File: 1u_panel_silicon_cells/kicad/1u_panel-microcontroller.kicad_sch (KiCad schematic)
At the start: 43 parts, among them J2 2-1734592-0, U1 TCAN330GDCNT, U11 TMP101NA/3KSLOTTED, U2 TMP101NA/3KSLOTTED, U7 STM32F091CCT7, X1 ECS-160-10-36Q-ES-TR

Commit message: fixed board outline, title blocks
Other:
- title: OreSat Solar Module (for Frame 2.0) -> OreSat Silicon Solar Module (for Frame 2.0)
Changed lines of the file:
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@@
 	(paper "USLedger")
 	(title_block
-		(title "OreSat Solar Module (for Frame 2.0)")
-		(date "2023-12-20")
-		(rev "6.0")
+		(title "OreSat Silicon Solar Module (for Frame 2.0)")
+		(date "2024-08-18")
+		(rev "1.0")
 	)
 	(junction

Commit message: updating remote repo for design review
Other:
- note added: "Solar module ID Required by CAN messages. 0: +X+Z 1: -Y+Z 2: -X+Z 3: -Y+Z 4: +X-Z .. and so on."
- note removed: "Solar module Serial Number Required by CAN messages. 0: +X+Z 1: -Y+Z 2: -X+Z 3: -Y+Z 4: +X-Z .. and so on."
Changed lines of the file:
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@@
 		)
 	)
-	(text "Solar module Serial Number\nRequired by CAN messages.\n0: +X+Z\n1: -Y+Z\n2: -X+Z\n3: -Y+Z\n4: +X-Z\n.. and so on."
+	(text "Solar module ID\nRequired by CAN messages.\n0: +X+Z\n1: -Y+Z\n2: -X+Z\n3: -Y+Z\n4: +X-Z\n.. and so on."
 		(exclude_from_sim no)
 		(at 226.06 215.9 0)

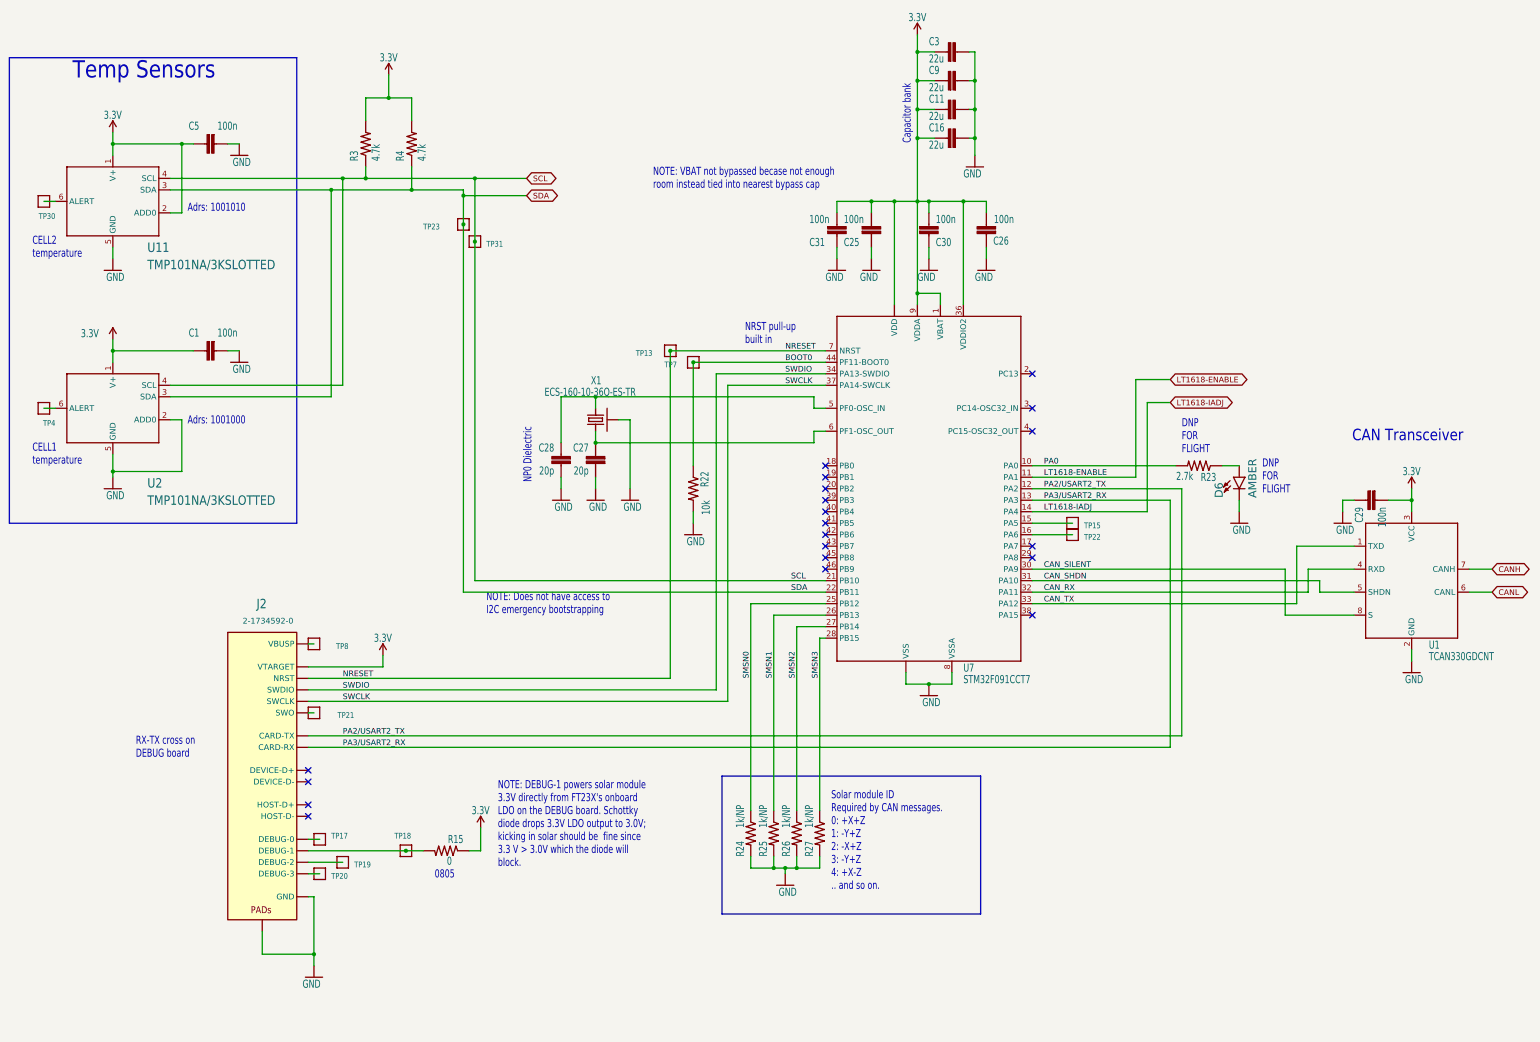
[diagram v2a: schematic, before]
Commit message: commiting silicon solar panel before moving programming header
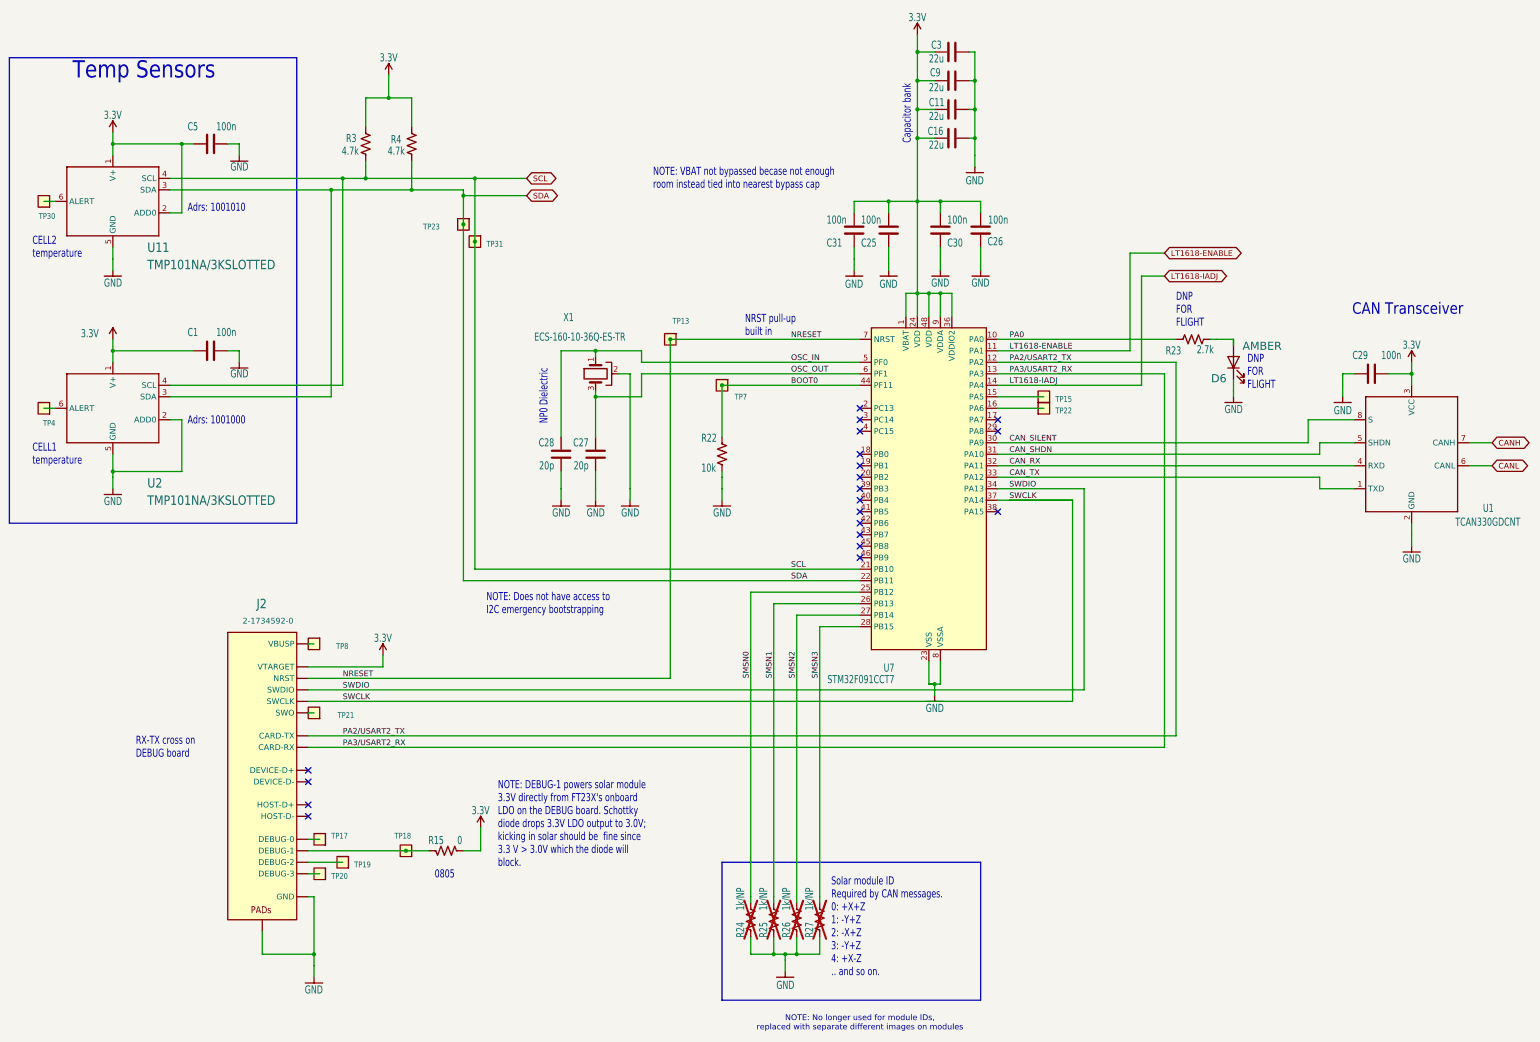
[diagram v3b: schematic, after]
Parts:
- C1, C25, C26, C27, C28, C29, C30, C31, C5: footprint 1u_panel:.0603-C-NOSILK -> oresat-passives:0603-C-NOSILK; symbol 1u_panel-eagle-import:oresat-rcl_C-EU0603-C-NOSILK -> Device:C
- C11, C16, C3, C9: footprint 1u_panel:.0805-B-NOSILK -> oresat-passives:0805-C-NOSILK; symbol 1u_panel-eagle-import:oresat-rcl_C-EU0805-B-NOSILK -> Device:C; DPN 1276-6817-1-ND -> 2571-GMC21X7R226M10NTTR-ND; MFR Samsung -> Cal-Chip; MPN CL32B226KOJVPNE -> GMC21X7R226M10NT
- D6: footprint 1u_panel:LED-0603 -> oresat-diodes:LED-0603; symbol 1u_panel-eagle-import:LED-GREEN0603 -> Device:LED
- R15: footprint 1u_panel:.0805-C-NOSILK -> oresat-passives:0805-C-NOSILK; symbol 1u_panel-eagle-import:R-US_0805-C-NOSILK -> Device:R_US
- R22: footprint 1u_panel:.0603-C-NOSILK -> oresat-passives:0603-C-NOSILK; symbol 1u_panel-eagle-import:R-US_0603-C-NOSILK -> Device:R_US; DPN A129693CT-ND -> RMCF0603JT10K0; MFR TE -> Stackpole; MPN CRGCQ0603F2K7 -> RMCF0603JT10K0
- R23, R3, R4: footprint 1u_panel:.0603-C-NOSILK -> oresat-passives:0603-C-NOSILK; symbol 1u_panel-eagle-import:R-US_0603-C-NOSILK -> Device:R_US
- R24, R25, R26, R27: footprint 1u_panel:.0603-C-NOSILK -> oresat-passives:0603-C-NOSILK; symbol 1u_panel-eagle-import:R-US_0603-C-NOSILK -> Device:R_US; now not fitted
- TP13, TP15, TP17, TP18, TP19, TP20, TP21, TP22, TP23, TP30, TP31, TP4, TP7, TP8: footprint 1u_panel:1X01 -> oresat-misc:TestPoint-0.75mm-th; symbol 1u_panel-eagle-import:TEST-POINT-LARGE-SQUARE -> oresat-misc:Test-Point-0.75mm-th; now left out of the parts list
- U1: footprint 1u_panel:SOT23-8_TI-DCN -> oresat-ics:SOT23-8_TI-DCN; symbol 1u_panel-eagle-import:TCAN330 -> oresat-ics:TCAN330; Distributor (none) -> DigiKey; MPN TCAN330GDCNT -> TCAN330GDCN
- U11, U2: footprint 1u_panel:DBV6-SLOT -> oresat-ics:DBV6-SLOT; symbol 1u_panel-eagle-import:TMP101NA/3KSLOTTED -> oresat-ics:TMP101NA
- U7: footprint 1u_panel:STM32F091C -> Package_QFP:LQFP-48_7x7mm_P0.5mm; symbol 1u_panel-eagle-import:STM32F091C -> MCU_ST_STM32F0:STM32F091CCUx
- X1: footprint 1u_panel:CRYSTAL_2.5X2 -> Crystal:Crystal_SMD_2520-4Pin_2.5x2.0mm; symbol 1u_panel-eagle-import:CRYSTAL-WITH-GND -> Device:Crystal_GND2
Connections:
- net 3.3V: now also R15.2; no longer R15.1
- net GND: no longer X1.4 (SHIELD)
- net at J2.18 (DEBUG-1), TP18.1: now also R15.1; no longer R15.2
- net OSC_IN: now reaches C28.1, U7.5 (PF0), X1.1
- net OSC_OUT: now reaches C27.1, U7.6 (PF1), X1.3
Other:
- note added: "NOTE: No longer used for module IDs, replaced with separate different images on modules"
- moved on the sheet: U1

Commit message: Updated all PN/DS/DPN/MPN/etc. for silicon solar module components
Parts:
- C1, C25, C26, C29, C30, C31, C5: DPN 1276-6985-1-ND -> 490-5798-2-ND; MFR Kemet -> Murata; MPN CL10B104KB85PND -> GCJ188R71H104KA12D
- C27, C28: DPN 490-11157-2-ND -> 490-1334-2-ND; MPN GCM1885C2A200JA16D -> GRM1885C2A200JA01D
- J2: DPN 732-11341-1-ND -> A100287TR-ND; MFR Wurth -> TE; MPN 687120183622 -> 2-1734592-0
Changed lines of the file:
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@@
 			)
 		)
-		(property "DPN" "732-11341-1-ND"
+		(property "DPN" "A100287TR-ND"
 			(at 100.33 189.23 0)
 			(effects
@@
 			)
 		)
-		(property "MFR" "Wurth"
+		(property "MFR" "TE"
 			(at 100.33 189.23 0)
 			(effects
@@
 			)
 		)
-		(property "MPN" "687120183622  "
+		(property "MPN" "2-1734592-0"
 			(at 100.33 189.23 0)
 			(effects
@@
 			)
 		)
-		(property "DPN" "1276-6985-1-ND"
+		(property "DPN" "490-5798-2-ND"
 			(at 88.9 50.8 0)
 			(effects
@@
 			)
 		)
-		(property "MFR" "Kemet"
+		(property "MFR" "Murata"
 			(at 88.9 50.8 0)
 			(effects
@@
 			)
 		)
-		(property "MPN" "CL10B104KB85PND"
+		(property "MPN" "GCJ188R71H104KA12D"
 			(at 88.9 50.8 0)
 			(effects
@@
 			)
 		)
-		(property "DPN" "1276-6985-1-ND"
+		(property "DPN" "490-5798-2-ND"
 			(at 231.14 69.85 0)
 			(effects
@@
 			)
 		)
-		(property "MFR" "Kemet"
+		(property "MFR" "Murata"
 			(at 231.14 69.85 0)
 			(effects
@@
 			)
 		)
-		(property "MPN" "CL10B104KB85PND"
+		(property "MPN" "GCJ188R71H104KA12D"
 			(at 231.14 69.85 0)
 			(effects
@@
 			)
 		)
-		(property "DPN" "490-11157-2-ND"
+		(property "DPN" "490-1334-2-ND"
 			(at 166.37 119.38 0)
 			(effects
@@
 			)
 		)
-		(property "MPN" "GCM1885C2A200JA16D"
+		(property "MPN" "GRM1885C2A200JA01D"
 			(at 166.37 119.38 0)
 			(effects
@@
 			)
 		)
-		(property "DPN" "1276-6985-1-ND"
+		(property "DPN" "490-5798-2-ND"
 			(at 88.9 96.52 0)
 			(effects
@@
 			)
 		)
-		(property "MFR" "Kemet"
+		(property "MFR" "Murata"
 			(at 88.9 96.52 0)
 			(effects
@@
 			)
 		)
-		(property "MPN" "CL10B104KB85PND"
+		(property "MPN" "GCJ188R71H104KA12D"
 			(at 88.9 96.52 0)
 			(effects
@@
 			)
 		)
-		(property "DPN" "1276-6985-1-ND"
+		(property "DPN" "490-5798-2-ND"
 			(at 250.19 69.85 0)
 			(effects
@@
 			)
 		)
-		(property "MFR" "Kemet"
+		(property "MFR" "Murata"
 			(at 250.19 69.85 0)
 			(effects
@@
 			)
 		)
-		(property "MPN" "CL10B104KB85PND"
+		(property "MPN" "GCJ188R71H104KA12D"
 			(at 250.19 69.85 0)
 			(effects
@@
 			)
 		)
-		(property "DPN" "490-11157-2-ND"
+		(property "DPN" "490-1334-2-ND"
 			(at 173.99 119.38 0)
 			(effects
@@
 			)
 		)
-		(property "MPN" "GCM1885C2A200JA16D"
+		(property "MPN" "GRM1885C2A200JA01D"
 			(at 173.99 119.38 0)
 			(effects
@@
 			)
 		)
-		(property "DPN" "1276-6985-1-ND"
+		(property "DPN" "490-5798-2-ND"
 			(at 345.44 101.6 0)
 			(effects
@@
 			)
 		)
-		(property "MFR" "Kemet"
+		(property "MFR" "Murata"
 			(at 345.44 101.6 0)
 			(effects
@@
 			)
 		)
-		(property "MPN" "CL10B104KB85PND"
+		(property "MPN" "GCJ188R71H104KA12D"
 			(at 345.44 101.6 0)
 			(effects
@@
 			)
 		)
-		(property "DPN" "1276-6985-1-ND"
+		(property "DPN" "490-5798-2-ND"
 			(at 238.76 69.85 0)
 			(effects
@@
 			)
 		)
-		(property "MFR" "Kemet"
+		(property "MFR" "Murata"
 			(at 238.76 69.85 0)
 			(effects
@@
 			)
 		)
-		(property "MPN" "CL10B104KB85PND"
+		(property "MPN" "GCJ188R71H104KA12D"
 			(at 238.76 69.85 0)
 			(effects
@@
 			)
 		)
-		(property "DPN" "1276-6985-1-ND"
+		(property "DPN" "490-5798-2-ND"
 			(at 259.08 69.85 0)
 			(effects
@@
 			)
 		)
-		(property "MFR" "Kemet"
+		(property "MFR" "Murata"
 			(at 259.08 69.85 0)
 			(effects
@@
 			)
 		)
-		(property "MPN" "CL10B104KB85PND"
+		(property "MPN" "GCJ188R71H104KA12D"
 			(at 259.08 69.85 0)
 			(effects

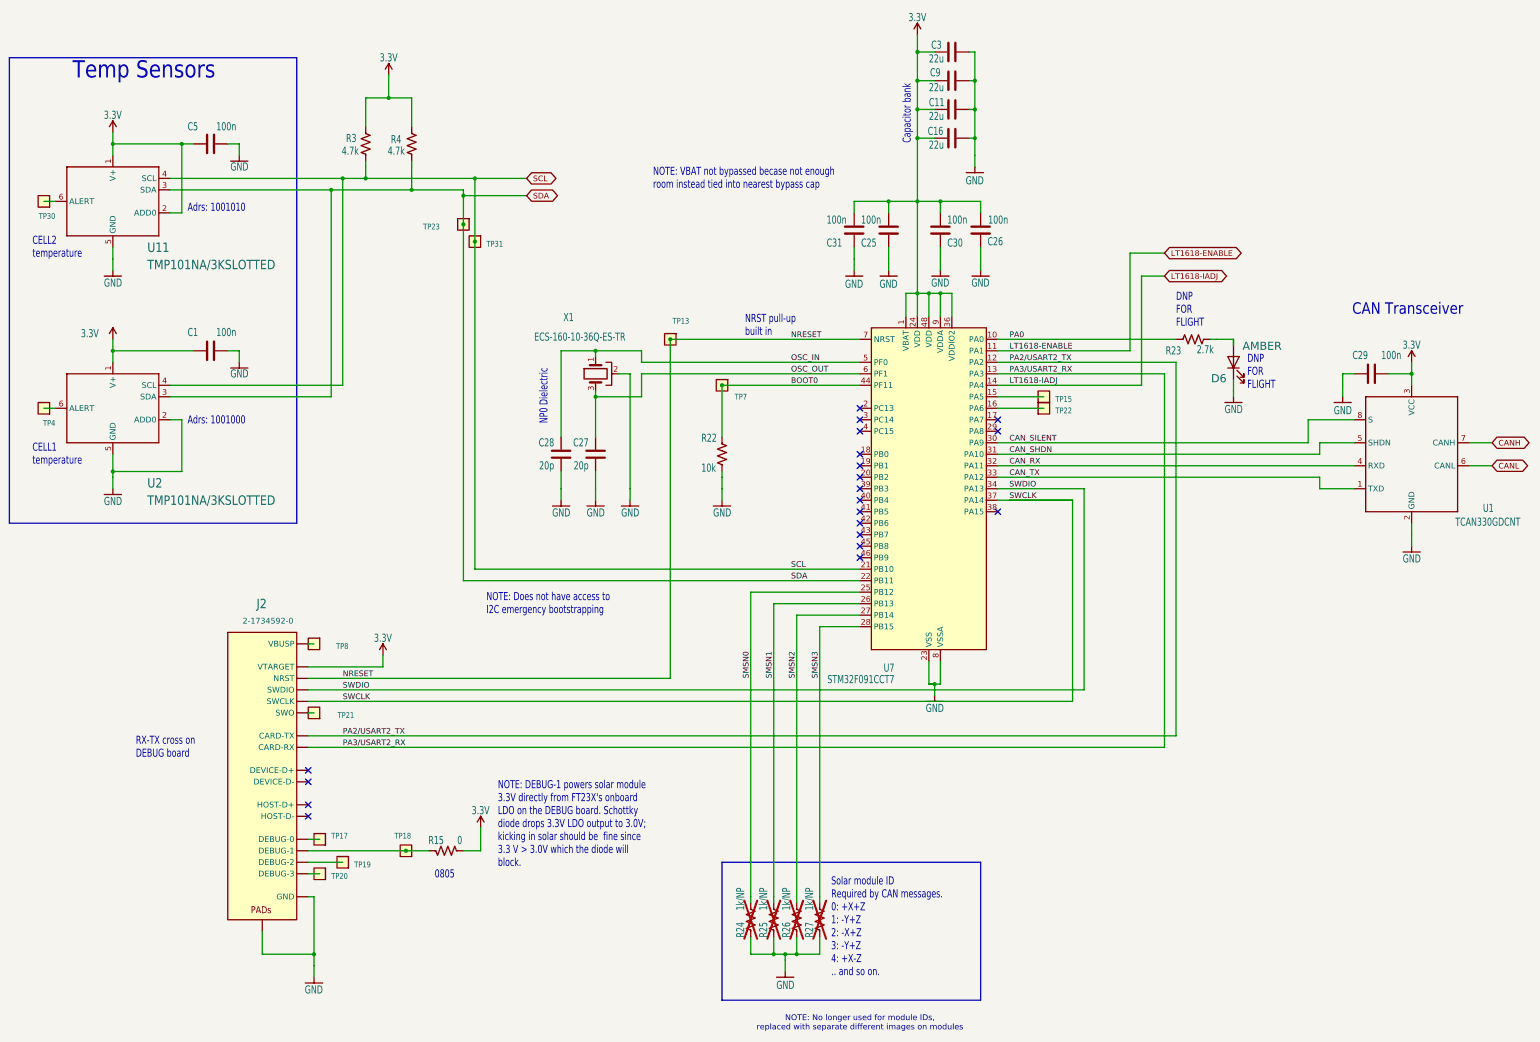
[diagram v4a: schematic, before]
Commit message: finished DR changes for silicon solar module
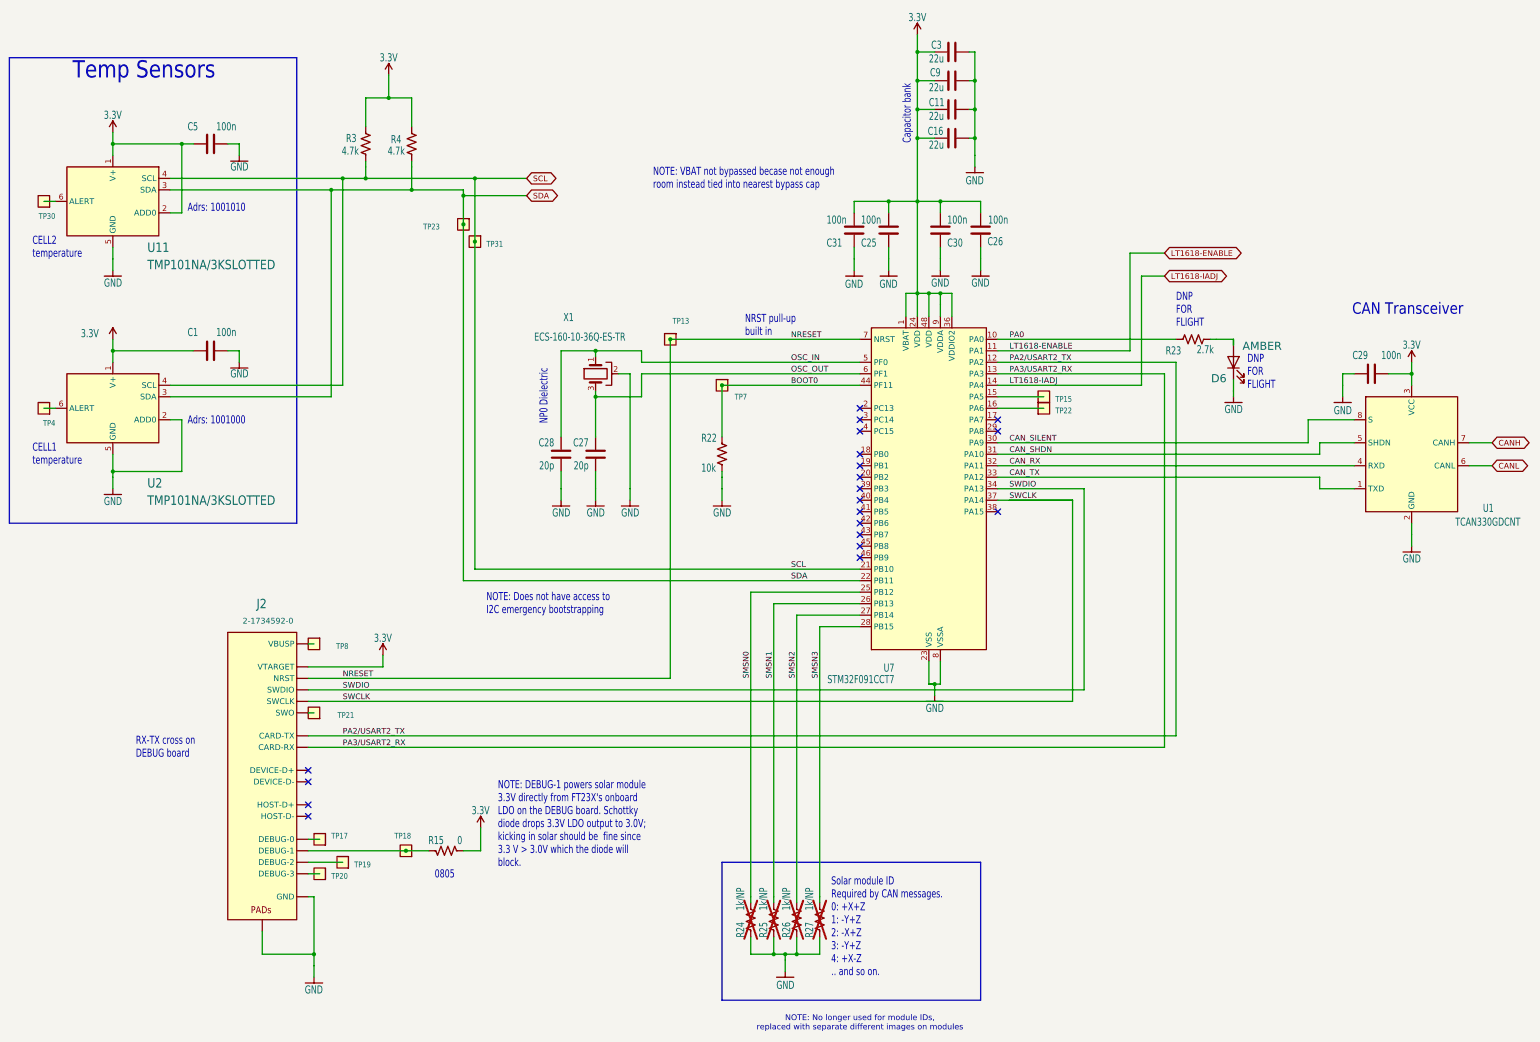
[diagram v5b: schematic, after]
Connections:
- net GND: now also D6.1 (K), U7.49 (VSS); no longer D6.C (K)
- net at R23.1: now also D6.2 (A); no longer D6.A
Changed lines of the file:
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@@
 		(pin "9"
+		)
+		(pin "49"
 		)
 		(instances
@@
 			)
 		)
-		(pin "A"
-		)
-		(pin "C"
-		)
-		(instances
+		(pin "1"
+		)
+		(pin "2"
+		)
+		(instances
